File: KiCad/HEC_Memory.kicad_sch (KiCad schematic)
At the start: 11 parts, among them U13 74LS245, U14 74LS245, U15 74LS32, U16 74LS32, U2 AS6C4008-55PCN, U22 74LS02, U3 AS6C4008-55PCN, U4 CY7C199, U41 74LS02, U5 CY7C199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

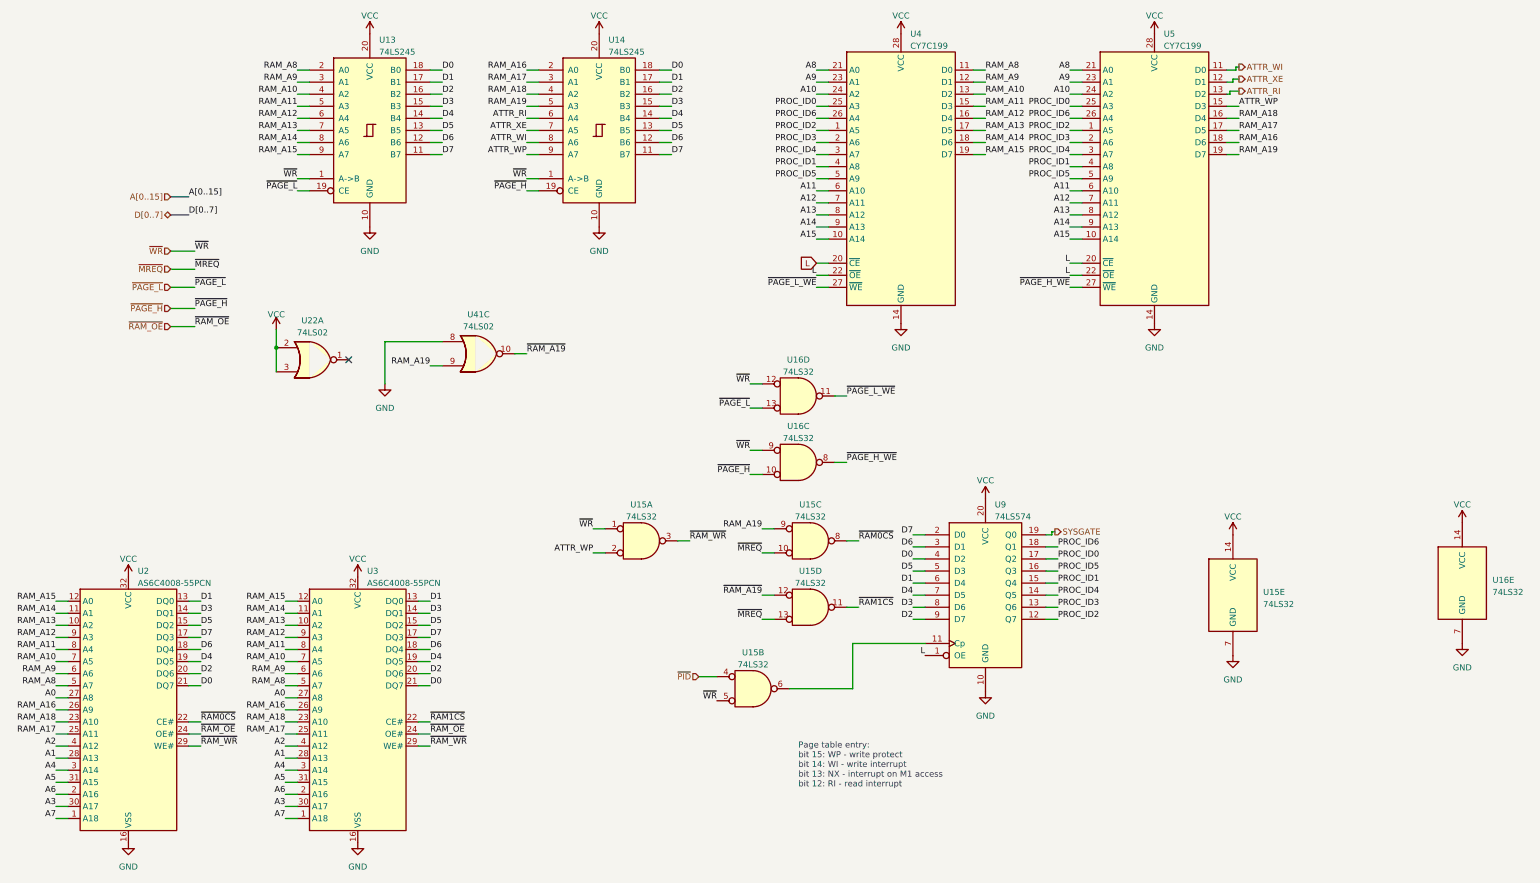
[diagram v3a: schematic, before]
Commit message: Protection Overhaul
Major change to the protection system. This change WILL break system software compatibility. Previously: bit 15: WP, 1=disable writing; bit 14: WI, 0=generate interrupt on write; bit 13: NX/XE 1/0=generate interrupt on M1 cycle; bit 12: RI 0=generate interrupt on read. New: bit 15: P, 0=not present, generate interrupt on MREQ access (any type of memory access except refresh); bit 14: WP, 0=read-only,1=read-write; bit 13: WI 0=generate interrupt on write; bit 12: XE 0=generate interrupt on M1.
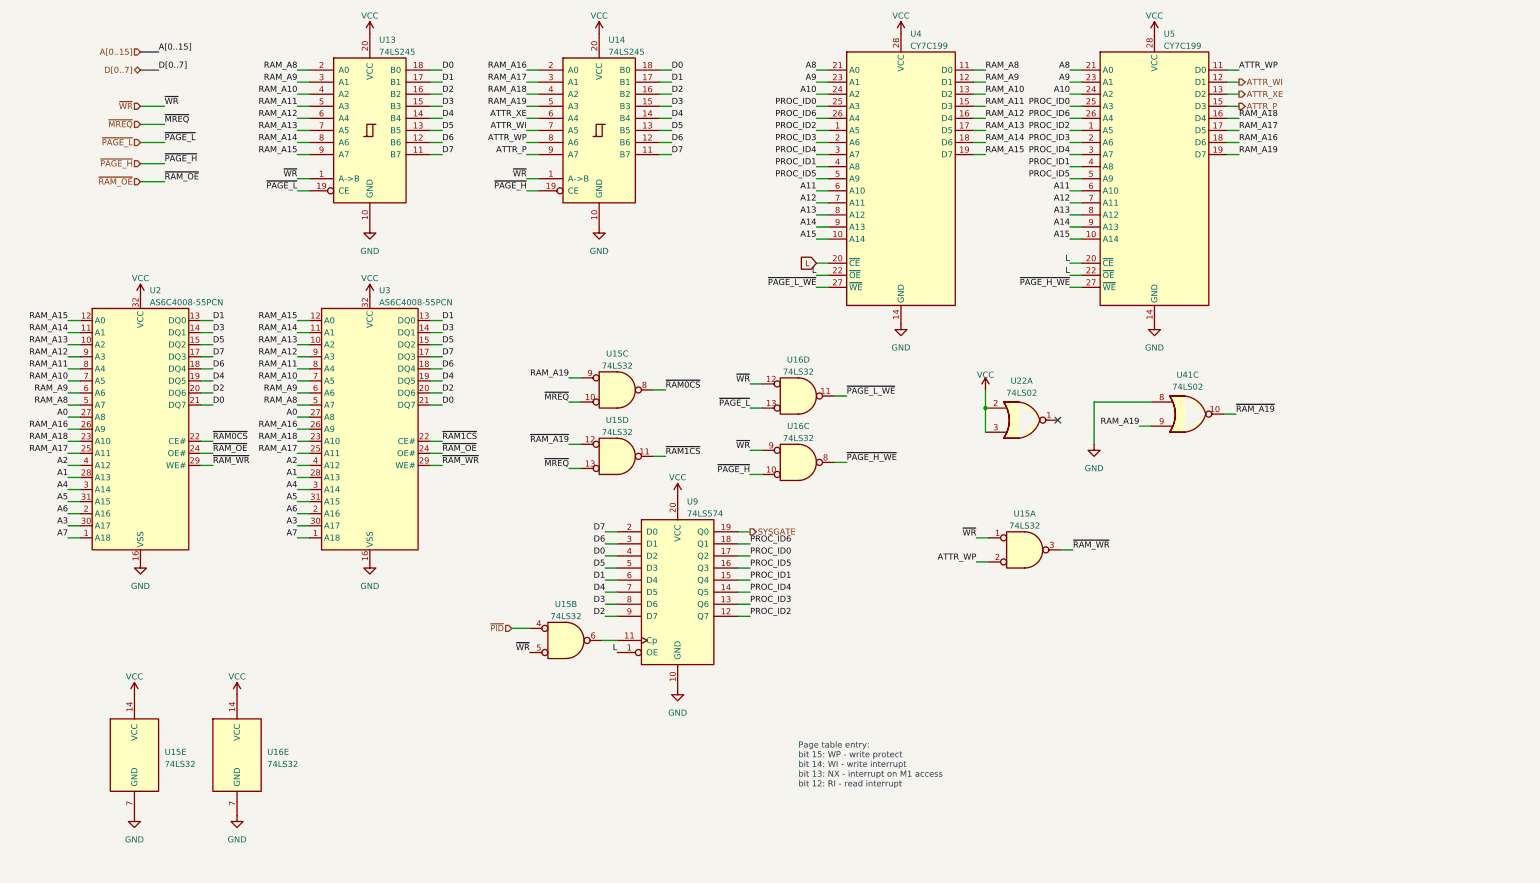
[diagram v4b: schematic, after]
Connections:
- net ATTR_RI is gone; now on net ATTR_XE: U14.6 (A4), U5.13 (D2)
- net ATTR_WI: now also U14.7 (A5), U5.12 (D1); no longer U14.8 (A6), U5.11 (D0)
- net ATTR_WP: now also U14.8 (A6), U5.11 (D0); no longer U14.9 (A7), U5.15 (D3)
- net ATTR_XE: no longer U14.7 (A5), U5.12 (D1)
- new net ATTR_P: U14.9 (A7), U5.15 (D3)
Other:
- moved on the sheet: U15A, U15B, U15C, U15D, U15E, U16E, U2, U22A, U3, U41C, U9

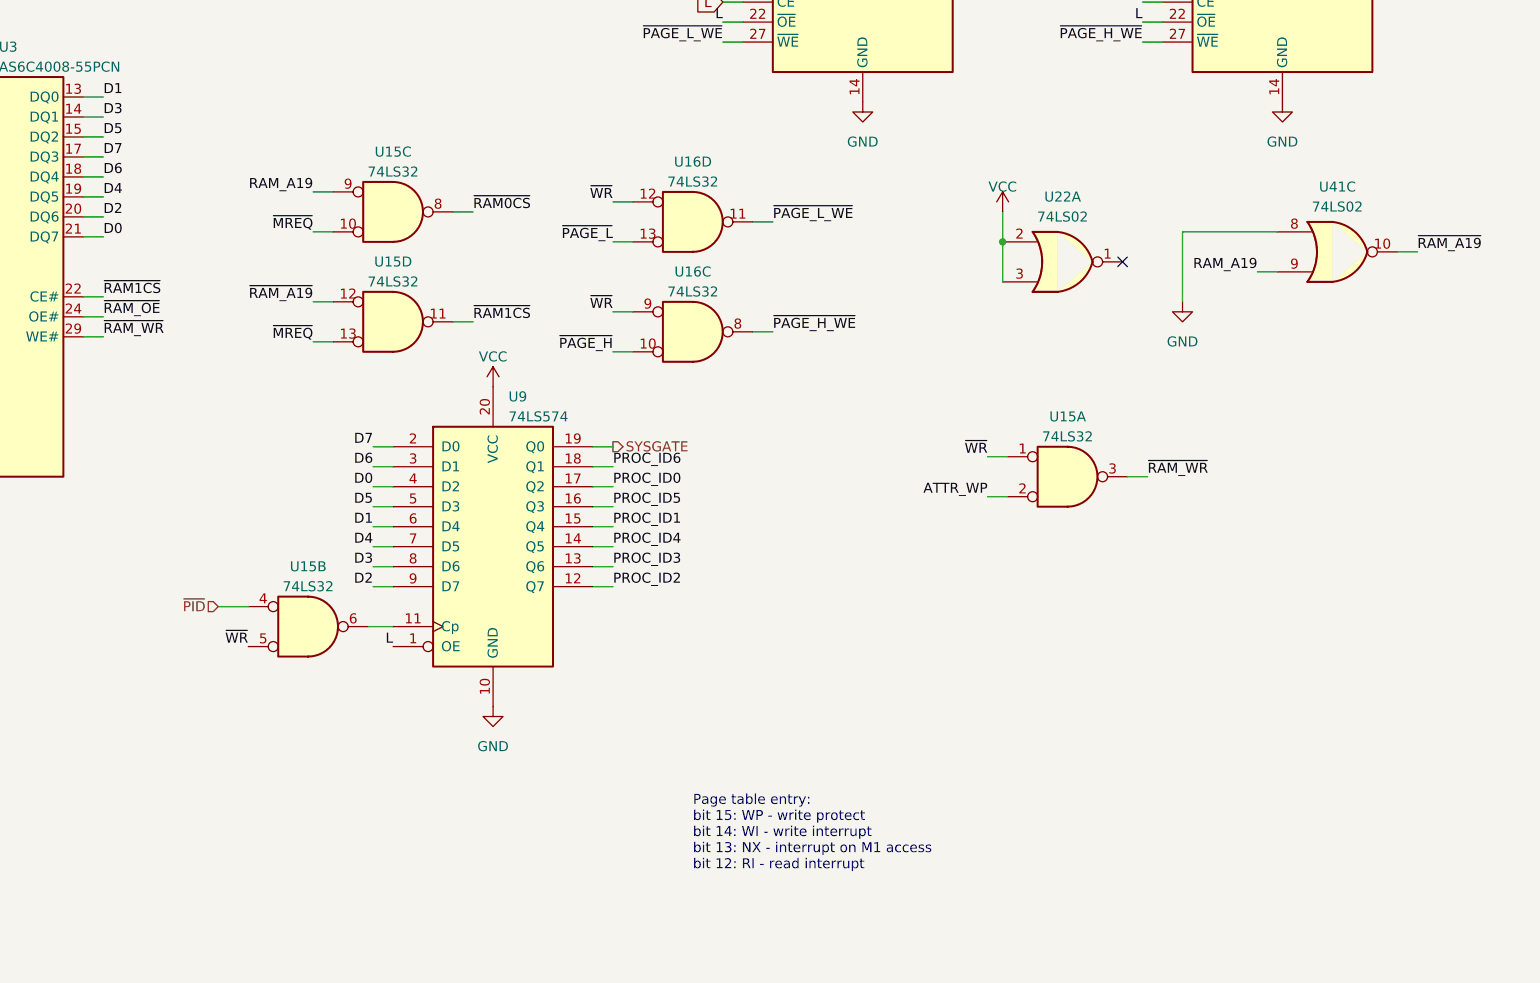
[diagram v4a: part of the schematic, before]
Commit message: Finish protection overhaul
Disable ram chip select when page is marked as not present, change write protect to 1 as write enabled, 0 as disabled. Change XE interrupt timings.
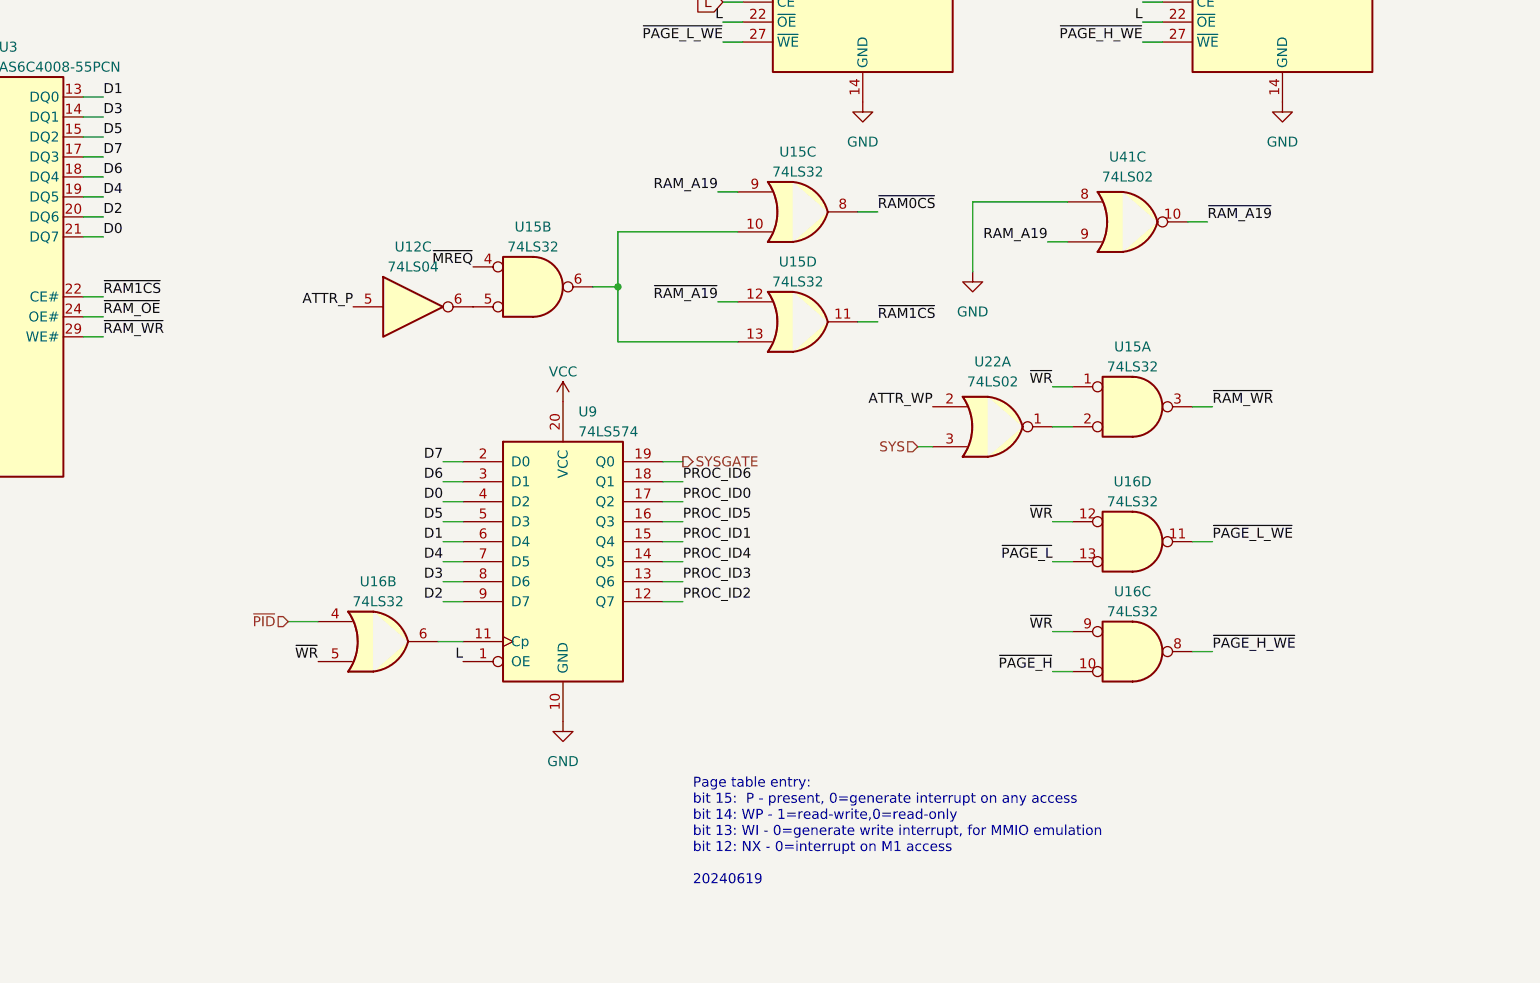
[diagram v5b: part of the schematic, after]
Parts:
- added U12: 74LS04, Library:DIP-14_W7.62mm_Socket_ThinPads, symbol 74xx:74LS04
- added unit 2 of U16
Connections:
- net ATTR_P: now also U12.5
- net ATTR_WP: now also U22.2; no longer U15.2
- net VCC: no longer U22.2, U22.3
- net ~{MREQ}: now also U15.4; no longer U15.10, U15.13
- net ~{PID}: now also U16.4; no longer U15.4
- net ~{WR}: now also U16.5; no longer U15.5
- net at U22.1: now also U15.2
- net at U15.6: now also U15.10, U15.13; no longer U9.11 (Cp)
- new net: U12.6, U15.5
- new net: U16.6, U9.11 (Cp)
- new net SYS: U22.3
- no-connect marks 1 -> 0
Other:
- note added: "Page table entry: bit 15: P - present, 0=generate interrupt on any access bit 14: WP - 1=read-write,0=read-only bit 13: WI - 0=generate write interrupt, for MMIO emulation bit 12: NX - 0=interrupt on M1 access 20240619"
- note removed: "Page table entry: bit 15: WP - write protect bit 14: WI - write interrupt bit 13: NX - interrupt on M1 access bit 12: RI - read interrupt"
- moved on the sheet: U15A, U15B, U16C, U16D, U22A, U41C, U9

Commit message: Spamming Net-ties
Spam Net-ties everywhere, replacing old H and L symbols in preparation for a 4-layber board design.
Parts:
- added NT17 (x3): NetTie_2, symbol Device:NetTie_2
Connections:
- net GND: now also NT17.1, NT17.1, NT17.1
- removed net L: U4.20 (~{CE}), U4.22 (~{OE}), U5.20 (~{CE}), U5.22 (~{OE}), U9.1 (OE)
- new net: NT17.2, U5.20 (~{CE}), U5.22 (~{OE})
- new net: NT17.2, U4.20 (~{CE}), U4.22 (~{OE})
- new net: NT17.2, U9.1 (OE)

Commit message: Add flash circuit
Changed EEPROM to NOR flash to increase speed. Added circuit to update firmware without requiring a programmer.
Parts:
- added NT17: NetTie_2, symbol Device:NetTie_2
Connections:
- net GND: now also NT17.1; no longer U41.8
- net ~{WR}: no longer U15.1
- new net: NT17.2, U41.8
- new net ~{NORMAL_WR}: U15.1
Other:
- moved on the sheet: NT17
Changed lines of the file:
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@@
+    (stroke (width 0) (type default))
+  )
+  (wire (pts (xy 226.06 111.76) (xy 226.06 117.475))
     (stroke (width 0) (type default))
   )
@@
     (stroke (width 0) (type default))
   )
-  (wire (pts (xy 149.86 152.4) (xy 149.86 158.115))
-    (stroke (width 0) (type default))
-  )
   (wire (pts (xy 218.44 30.48) (xy 215.9 30.48))
     (stroke (width 0) (type default))
@@
     (stroke (width 0) (type default))
   )
+  (wire (pts (xy 214.63 93.98) (xy 217.805 93.98))
+    (stroke (width 0) (type default))
+  )
   (wire (pts (xy 182.88 55.88) (xy 185.42 55.88))
     (stroke (width 0) (type default))
@@
     (stroke (width 0) (type default))
   )
+  (wire (pts (xy 149.86 154.94) (xy 149.86 152.4))
+    (stroke (width 0) (type default))
+  )
   (wire (pts (xy 25.4 126.365) (xy 27.94 126.365))
     (stroke (width 0) (type default))
@@
     (stroke (width 0) (type default))
   )
+  (wire (pts (xy 222.885 93.98) (xy 226.695 93.98))
+    (stroke (width 0) (type default))
+  )
   (wire (pts (xy 124.46 35.56) (xy 121.92 35.56))
     (stroke (width 0) (type default))
@@
     (stroke (width 0) (type default))
   )
+  (wire (pts (xy 40.005 32.385) (xy 45.72 32.385))
+    (stroke (width 0) (type default))
+  )
   (wire (pts (xy 224.79 139.7) (xy 227.33 139.7))
     (stroke (width 0) (type default))
@@
     (stroke (width 0) (type default))
   )
+  (wire (pts (xy 147.955 154.94) (xy 149.86 154.94))
+    (stroke (width 0) (type default))
+  )
   (wire (pts (xy 25.4 118.745) (xy 27.94 118.745))
     (stroke (width 0) (type default))
@@
     (stroke (width 0) (type default))
   )
+  (wire (pts (xy 226.06 117.475) (xy 227.33 117.475))
+    (stroke (width 0) (type default))
+  )
   (wire (pts (xy 101.6 90.805) (xy 104.14 90.805))
     (stroke (width 0) (type default))
@@
     (stroke (width 0) (type default))
   )
-  (wire (pts (xy 214.63 93.98) (xy 226.695 93.98))
-    (stroke (width 0) (type default))
-  )
   (wire (pts (xy 40.64 39.37) (xy 45.72 39.37))
     (stroke (width 0) (type default))
@@
     (stroke (width 0) (type default))
   )
-  (wire (pts (xy 224.79 117.475) (xy 227.33 117.475))
-    (stroke (width 0) (type default))
-  )
   (wire (pts (xy 53.34 111.125) (xy 55.88 111.125))
     (stroke (width 0) (type default))
@@
   )
   (wire (pts (xy 242.57 151.13) (xy 245.11 151.13))
+    (stroke (width 0) (type default))
+  )
+  (wire (pts (xy 142.875 154.94) (xy 142.875 158.115))
     (stroke (width 0) (type default))
   )
@@
     (effects (font (size 1.27 1.27)) (justify right bottom))
   )
+  (label "~{NORMAL_WR}" (at 226.06 111.76 180) (fields_autoplaced)
+    (effects (font (size 1.27 1.27)) (justify right bottom))
+  )
   (label "RAM_A9" (at 218.44 30.48 0) (fields_autoplaced)
     (effects (font (size 1.27 1.27)) (justify left bottom))
@@
     (effects (font (size 1.27 1.27)) (justify right bottom))
   )
-  (label "~{WR}" (at 224.79 117.475 180) (fields_autoplaced)
-    (effects (font (size 1.27 1.27)) (justify right bottom))
-  )
   (label "RAM_A10" (at 218.44 33.02 0) (fields_autoplaced)
     (effects (font (size 1.27 1.27)) (justify left bottom))
@@
   (label "RAM_A16" (at 73.66 103.505 180) (fields_autoplaced)
     (effects (font (size 1.27 1.27)) (justify right bottom))
+  )
+  (label "~{NORMAL_WR}" (at 45.72 32.385 0) (fields_autoplaced)
+    (effects (font (size 1.27 1.27)) (justify left bottom))
   )
   (label "~{RAM_OE}" (at 55.88 108.585 0) (fields_autoplaced)
@@
   )
   (hierarchical_label "SYS" (shape input) (at 207.645 125.095 180) (fields_autoplaced)
+    (effects (font (size 1.27 1.27)) (justify right))
+  )
+  (hierarchical_label "~{NORMAL_WR}" (shape input) (at 40.005 32.385 180) (fields_autoplaced)
     (effects (font (size 1.27 1.27)) (justify right))
   )
@@
     )
   )
-  (symbol (lib_id "Device:NetTie_2") (at 147.32 158.115 0) (unit 1)
+  (symbol (lib_id "Device:NetTie_2") (at 145.415 154.94 0) (unit 1)
     (in_bom no) (on_board yes) (dnp no) (fields_autoplaced)
-    (property "Reference" "NT17" (at 147.32 154.305 0)
-      (effects (font (size 1.27 1.27)))
-    )
-    (property "Value" "NetTie_2" (at 147.32 156.845 0)
-      (effects (font (size 1.27 1.27)))
-    )
-    (property "Footprint" "" (at 147.32 158.115 0)
-      (effects (font (size 1.27 1.27)) hide)
-    )
-    (property "Datasheet" "~" (at 147.32 158.115 0)
+    (property "Reference" "NT17" (at 145.415 151.13 0)
+      (effects (font (size 1.27 1.27)))
+    )
+    (property "Value" "NetTie_2" (at 145.415 153.67 0)
+      (effects (font (size 1.27 1.27)))
+    )
+    (property "Footprint" "" (at 145.415 154.94 0)
+      (effects (font (size 1.27 1.27)) hide)
+    )
+    (property "Datasheet" "~" (at 145.415 154.94 0)
       (effects (font (size 1.27 1.27)) hide)
     )
@@
     )
   )
+  (symbol (lib_id "Device:NetTie_2") (at 220.345 93.98 0) (unit 1)
+    (in_bom no) (on_board yes) (dnp no) (fields_autoplaced)
+    (property "Reference" "NT17" (at 220.345 90.17 0)
+      (effects (font (size 1.27 1.27)))
+    )
+    (property "Value" "NetTie_2" (at 220.345 92.71 0)
+      (effects (font (size 1.27 1.27)))
+    )
+    (property "Footprint" "" (at 220.345 93.98 0)
+      (effects (font (size 1.27 1.27)) hide)
+    )
+    (property "Datasheet" "~" (at 220.345 93.98 0)
+      (effects (font (size 1.27 1.27)) hide)
+    )
+    (pin "1")
+    (pin "2")
+    (instances
+      (project "HEC1"
+        (path "/87935374-b60a-4f41-99da-94b76103dd77/73a0c68b-1e42-4c0d-ae31-b1a96d0648bb"
+          (reference "NT17") (unit 1)
+        )
+        (path "/87935374-b60a-4f41-99da-94b76103dd77/933a6f90-eb98-4eb1-8c19-8a76228aece1"
+          (reference "NT29") (unit 1)
+        )
+      )
+    )
+  )
   (symbol (lib_id "74xx:74LS32") (at 192.405 95.25 0) (unit 3)
     (in_bom yes) (on_board yes) (dnp no) (fields_autoplaced)
@@
     )
   )
-  (symbol (lib_id "power:GND") (at 144.78 158.115 0) (unit 1)
-    (in_bom yes) (on_board yes) (dnp no) (fields_autoplaced)
-    (property "Reference" "#PWR0164" (at 144.78 164.465 0)
-      (effects (font (size 1.27 1.27)) hide)
-    )
-    (property "Value" "GND" (at 144.78 163.195 0)
-      (effects (font (size 1.27 1.27)))
-    )
-    (property "Footprint" "" (at 144.78 158.115 0)
-      (effects (font (size 1.27 1.27)) hide)
-    )
-    (property "Datasheet" "" (at 144.78 158.115 0)
-      (effects (font (size 1.27 1.27)) hide)
-    )
+  (symbol (lib_id "power:GND") (at 142.875 158.115 0) (unit 1)
+    (in_bom yes) (on_board yes) (dnp no) (fields_autoplaced)
+    (property "Reference" "#PWR0164" (at 142.875 164.465 0)
+      (effects (font (size 1.27 1.27)) hide)
+    )
+    (property "Value" "GND" (at 142.875 163.195 0)
+      (effects (font (size 1.27 1.27)))
+    )
+    (property "Footprint" "" (at 142.875 158.115 0)
+      (effects (font (size 1.27 1.27)) hide)
+    )
+    (property "Datasheet" "" (at 142.875 158.115 0)
+      (effects (font (size 1.27 1.27)) hide)
+    )

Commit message: Updates to schematic
Unfinished design of V2 schematic
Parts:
- NT23, NT24, NT25, NT29: renamed from NT17; footprint (none) -> NetTie:NetTie-2_SMD_Pad0.5mm
- U2, U3: footprint Library:DIP-32_W15.24mm_Socket_ThinPads -> Package_DIP:DIP-32_W15.24mm
